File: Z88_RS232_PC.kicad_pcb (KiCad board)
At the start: 2 copper layers, 30 x 7.9 mm, 3 parts, among them J1 DE9_Male, J2 DE9_Male

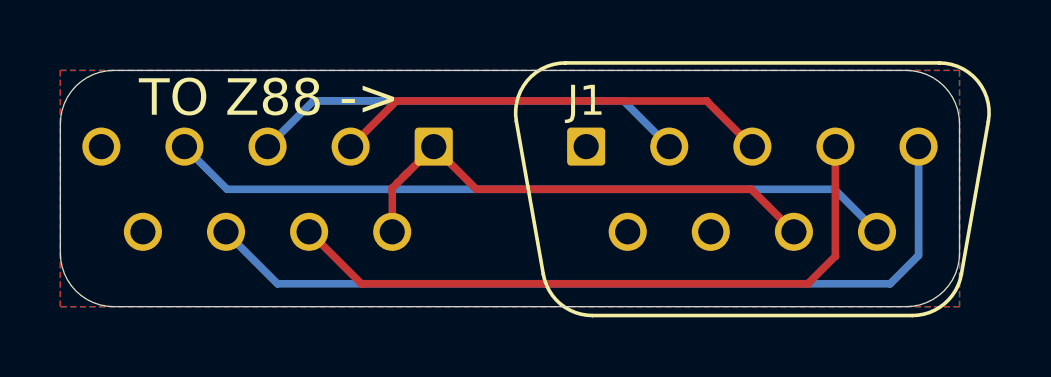
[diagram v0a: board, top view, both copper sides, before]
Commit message: kicad8, increase model-t pcb size
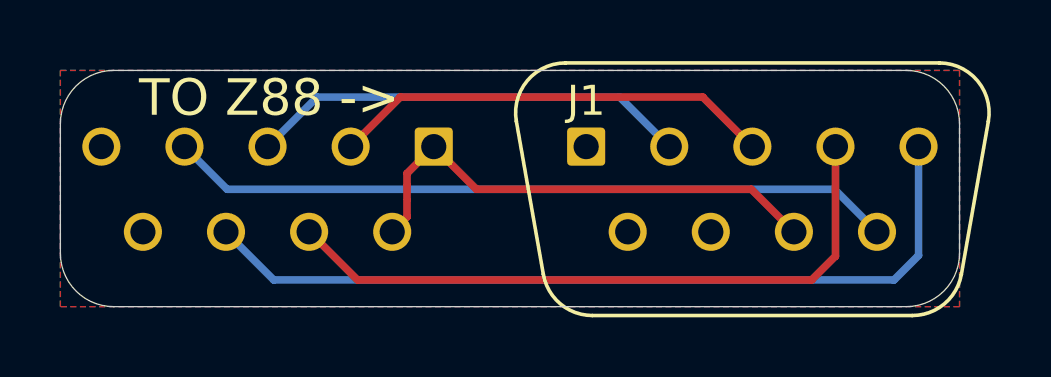
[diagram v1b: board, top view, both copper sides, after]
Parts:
- moved NT1 0.51 mm to (136.3, 98.0), turned to -90 degrees
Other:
- net class Default removed
